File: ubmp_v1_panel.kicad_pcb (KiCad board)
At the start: 2 copper layers, 131 x 113.5 mm, 312 parts, among them J1 Conn_02x05_Counter_Clockwise, J2 USB_A, U1 NUF8401MNT4G, U2 MIC5245-3.3, U3 STM32F103CBUx, U4 NUF2042XV6T1G, Y1 PRQC8.00CR1010V00L

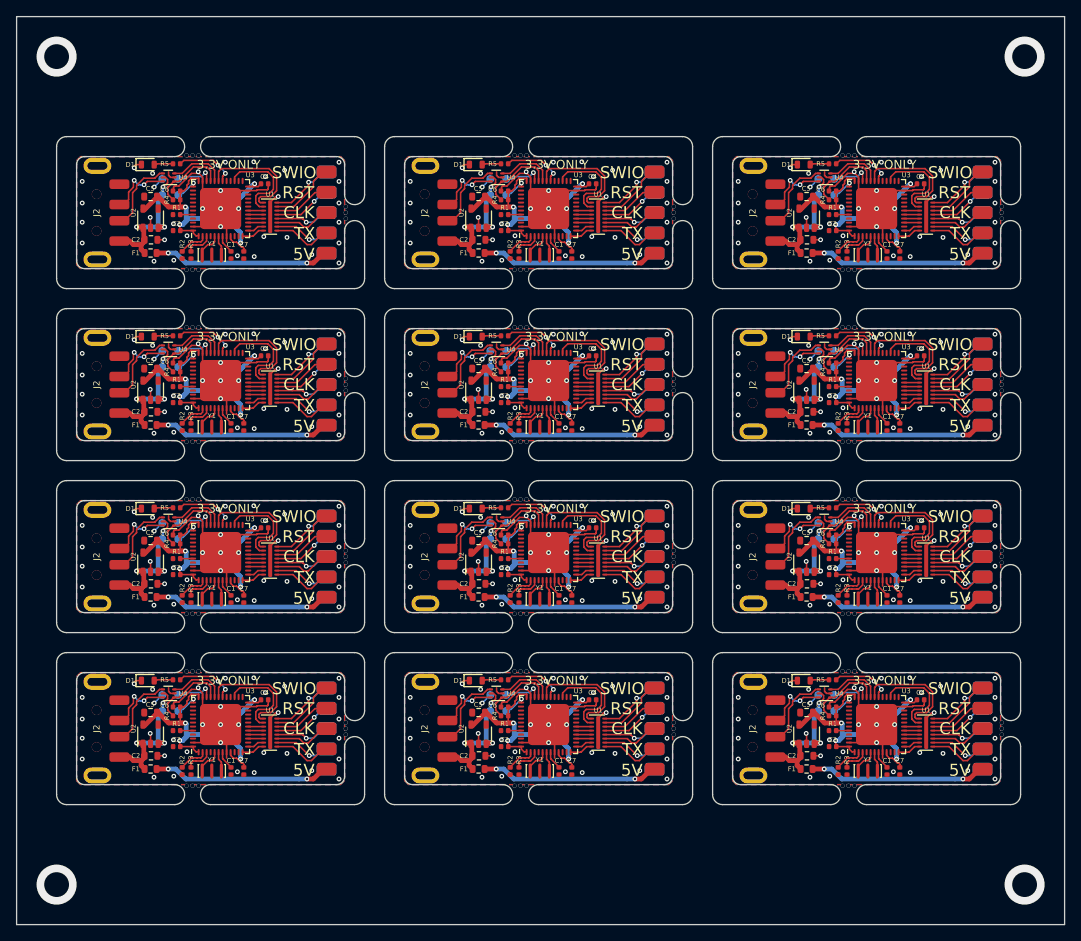
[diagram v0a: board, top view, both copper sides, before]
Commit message: Updated USBPCB version and panel
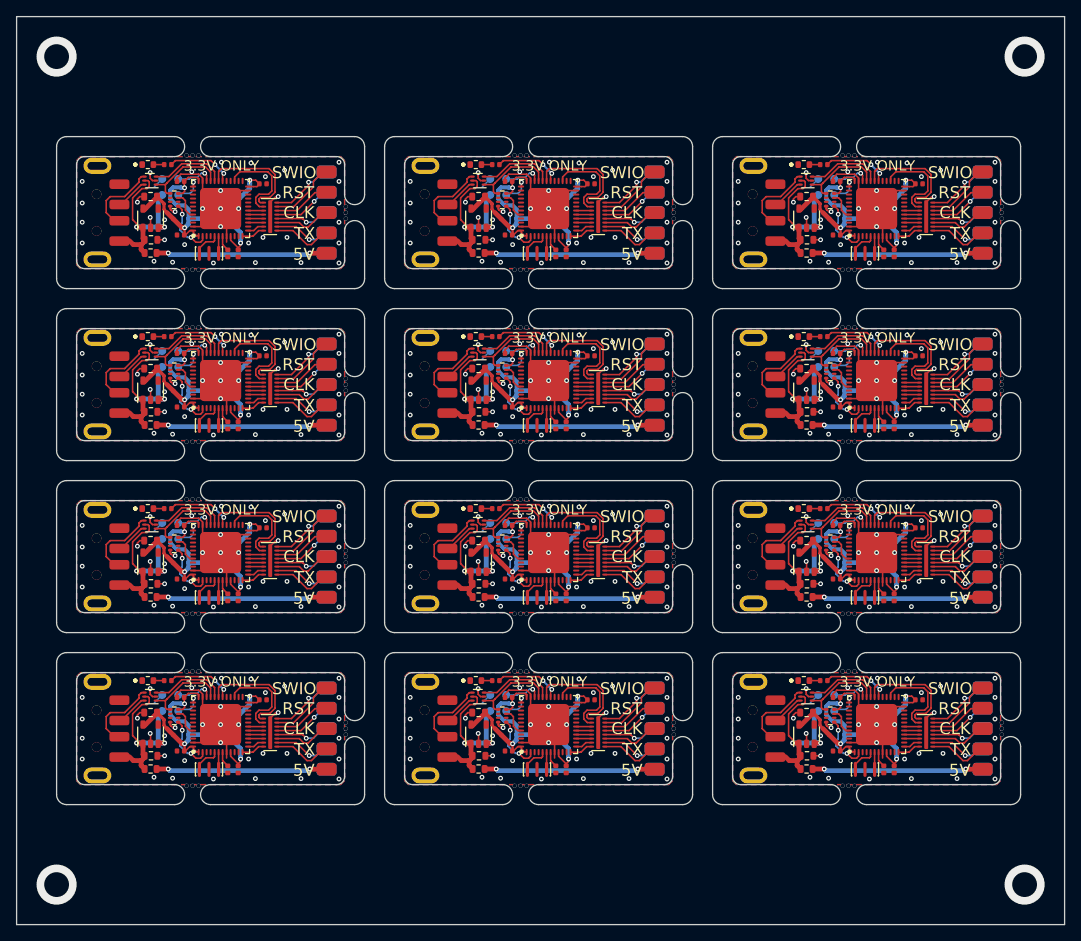
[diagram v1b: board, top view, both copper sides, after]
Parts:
- removed the C1 at (177.8, 64.3)
- removed the C1 at (177.8, 128.8)
- removed the C1 at (136.8, 128.8)
- removed the C1 at (95.8, 128.8)
- removed the C1 at (136.8, 64.3)
- removed the C1 at (95.8, 64.3)
- removed the C1 at (177.8, 85.8)
- removed the C1 at (136.8, 85.8)
- removed the C1 at (95.8, 85.8)
- removed the C1 at (177.8, 107.3)
- removed the C1 at (136.8, 107.3)
- removed the C1 at (95.8, 107.3)
- removed the C3 at (171.0, 61.2)
- removed the C3 at (171.0, 125.8)
- removed the C3 at (130.0, 125.8)
- removed the C3 at (89.0, 125.8)
- removed the C3 at (130.0, 61.2)
- removed the C3 at (89.0, 61.2)
- removed the C3 at (171.0, 82.8)
- removed the C3 at (130.0, 82.8)
- removed the C3 at (89.0, 82.8)
- removed the C3 at (171.0, 104.2)
- removed the C3 at (130.0, 104.2)
- removed the C3 at (89.0, 104.2)
- removed the C4 at (141.0, 55.4)
- removed the C4 at (182.0, 119.9)
- removed the C4 at (141.0, 119.9)
- removed the C4 at (100.0, 119.9)
- removed the C4 at (182.0, 55.4)
- removed the C4 at (100.0, 55.4)
- removed the C4 at (141.0, 76.9)
- removed the C4 at (182.0, 76.9)
- removed the C4 at (100.0, 76.9)
- removed the C4 at (141.0, 98.4)
- removed the C4 at (182.0, 98.4)
- removed the C4 at (100.0, 98.4)
- removed the C6 at (130.0, 56.3)
- removed the C6 at (171.0, 120.8)
- removed the C6 at (130.0, 120.8)
- removed the C6 at (89.0, 120.8)
- removed the C6 at (171.0, 56.3)
- removed the C6 at (89.0, 56.3)
- removed the C6 at (130.0, 77.8)
- removed the C6 at (171.0, 77.8)
- removed the C6 at (89.0, 77.8)
- removed the C6 at (130.0, 99.3)
- removed the C6 at (171.0, 99.3)
- removed the C6 at (89.0, 99.3)
- removed the C7 at (179.4, 64.3)
- removed the C7 at (179.4, 128.8)
- removed the C7 at (138.4, 128.8)
- removed the C7 at (97.4, 128.8)
- removed the C7 at (138.4, 64.3)
- removed the C7 at (97.4, 64.3)
- removed the C7 at (179.4, 85.8)
- removed the C7 at (138.4, 85.8)
- removed the C7 at (97.4, 85.8)
- removed the C7 at (179.4, 107.3)
- removed the C7 at (138.4, 107.3)
- removed the C7 at (97.4, 107.3)
- removed the D1 at (167.4, 53.0)
- removed the D1 at (167.4, 117.5)
- removed the D1 at (126.4, 117.5)
- removed the D1 at (85.4, 117.5)
- removed the D1 at (126.4, 53.0)
- removed the D1 at (85.4, 53.0)
- removed the D1 at (167.4, 74.5)
- removed the D1 at (126.4, 74.5)
- removed the D1 at (85.4, 74.5)
- removed the D1 at (167.4, 96.0)
- removed the D1 at (126.4, 96.0)
- removed the D1 at (85.4, 96.0)
- removed the R1 at (130.0, 59.2)
- removed the R1 at (171.0, 123.8)
- removed the R1 at (130.0, 123.8)
- removed the R1 at (89.0, 123.8)
- removed the R1 at (171.0, 59.2)
- removed the R1 at (89.0, 59.2)
- removed the R1 at (130.0, 80.8)
- removed the R1 at (171.0, 80.8)
- removed the R1 at (89.0, 80.8)
- removed the R1 at (130.0, 102.2)
- removed the R1 at (171.0, 102.2)
- removed the R1 at (89.0, 102.2)
- removed R2 (x12), R3 (x12), R4 (x12): 1.5k, passive:R_0402_1005Metric_Rounded
- removed R5 (x12): 470, passive:R_0402_1005Metric_Rounded
- removed the REF** at (137.5, 56.0)
- removed the REF** at (178.5, 120.5)
- removed the REF** at (137.5, 120.5)
- removed the REF** at (96.5, 120.5)
- removed the REF** at (178.5, 56.0)
- removed the REF** at (96.5, 56.0)
- removed the REF** at (137.5, 77.5)
- removed the REF** at (178.5, 77.5)
- removed the REF** at (96.5, 77.5)
- removed the REF** at (137.5, 99.0)
- removed the REF** at (178.5, 99.0)
- removed the REF** at (96.5, 99.0)
- removed the U4 at (129.0, 54.6)
- removed the U4 at (170.0, 119.1)
- removed the U4 at (129.0, 119.1)
- removed the U4 at (88.0, 119.1)
- removed the U4 at (170.0, 54.6)
- removed the U4 at (88.0, 54.6)
- removed the U4 at (129.0, 76.1)
- removed the U4 at (170.0, 76.1)
- removed the U4 at (88.0, 76.1)
- removed the U4 at (129.0, 97.6)
- removed the U4 at (170.0, 97.6)
- removed the U4 at (88.0, 97.6)
- removed the Y1 at (175.4, 64.3)
- removed the Y1 at (175.4, 128.8)
- removed the Y1 at (134.4, 128.8)
- removed the Y1 at (93.4, 128.8)
- removed the Y1 at (134.4, 64.3)
- removed the Y1 at (93.4, 64.3)
- removed the Y1 at (175.4, 85.8)
- removed the Y1 at (134.4, 85.8)
- removed the Y1 at (93.4, 85.8)
- removed the Y1 at (175.4, 107.3)
- removed the Y1 at (134.4, 107.3)
- removed the Y1 at (93.4, 107.3)
- added C1: 100n, passive:C_0402_1005Metric_Rounded, F.Cu at (95.4, 64.1)
- added C1: 100n, passive:C_0402_1005Metric_Rounded, F.Cu at (177.4, 128.6)
- added C1: 100n, passive:C_0402_1005Metric_Rounded, F.Cu at (136.4, 128.6)
- added C1: 100n, passive:C_0402_1005Metric_Rounded, F.Cu at (95.4, 128.6)
- added C1: 100n, passive:C_0402_1005Metric_Rounded, F.Cu at (136.4, 64.1)
- added C1: 100n, passive:C_0402_1005Metric_Rounded, F.Cu at (177.4, 64.1)
- added C1: 100n, passive:C_0402_1005Metric_Rounded, F.Cu at (95.4, 85.6)
- added C1: 100n, passive:C_0402_1005Metric_Rounded, F.Cu at (136.4, 85.6)
- added C1: 100n, passive:C_0402_1005Metric_Rounded, F.Cu at (177.4, 85.6)
- added C1: 100n, passive:C_0402_1005Metric_Rounded, F.Cu at (95.4, 107.1)
- added C1: 100n, passive:C_0402_1005Metric_Rounded, F.Cu at (136.4, 107.1)
- added C1: 100n, passive:C_0402_1005Metric_Rounded, F.Cu at (177.4, 107.1)
- added C3: 100n, passive:C_0402_1005Metric_Rounded, F.Cu at (130.5, 61.8)
- added C3: 100n, passive:C_0402_1005Metric_Rounded, F.Cu at (171.5, 126.3)
- added C3: 100n, passive:C_0402_1005Metric_Rounded, F.Cu at (130.5, 126.3)
- added C3: 100n, passive:C_0402_1005Metric_Rounded, F.Cu at (89.5, 126.3)
- added C3: 100n, passive:C_0402_1005Metric_Rounded, F.Cu at (89.5, 61.8)
- added C3: 100n, passive:C_0402_1005Metric_Rounded, F.Cu at (171.5, 61.8)
- added C3: 100n, passive:C_0402_1005Metric_Rounded, F.Cu at (130.5, 83.3)
- added C3: 100n, passive:C_0402_1005Metric_Rounded, F.Cu at (89.5, 83.3)
- added C3: 100n, passive:C_0402_1005Metric_Rounded, F.Cu at (171.5, 83.3)
- added C3: 100n, passive:C_0402_1005Metric_Rounded, F.Cu at (130.5, 104.8)
- added C3: 100n, passive:C_0402_1005Metric_Rounded, F.Cu at (89.5, 104.8)
- added C3: 100n, passive:C_0402_1005Metric_Rounded, F.Cu at (171.5, 104.8)
- added C4: 100n, passive:C_0402_1005Metric_Rounded, F.Cu at (140.8, 55.4)
- added C4: 100n, passive:C_0402_1005Metric_Rounded, F.Cu at (181.8, 119.9)
- added C4: 100n, passive:C_0402_1005Metric_Rounded, F.Cu at (140.8, 119.9)
- added C4: 100n, passive:C_0402_1005Metric_Rounded, F.Cu at (99.8, 119.9)
- added C4: 100n, passive:C_0402_1005Metric_Rounded, F.Cu at (99.8, 55.4)
- added C4: 100n, passive:C_0402_1005Metric_Rounded, F.Cu at (181.8, 55.4)
- added C4: 100n, passive:C_0402_1005Metric_Rounded, F.Cu at (140.8, 76.9)
- added C4: 100n, passive:C_0402_1005Metric_Rounded, F.Cu at (99.8, 76.9)
- added C4: 100n, passive:C_0402_1005Metric_Rounded, F.Cu at (181.8, 76.9)
- added C4: 100n, passive:C_0402_1005Metric_Rounded, F.Cu at (140.8, 98.4)
- added C4: 100n, passive:C_0402_1005Metric_Rounded, F.Cu at (99.8, 98.4)
- added C4: 100n, passive:C_0402_1005Metric_Rounded, F.Cu at (181.8, 98.4)
- added C6: 100n, passive:C_0402_1005Metric_Rounded, F.Cu at (89.5, 55.1)
- added C6: 100n, passive:C_0402_1005Metric_Rounded, F.Cu at (171.5, 119.6)
- added C6: 100n, passive:C_0402_1005Metric_Rounded, F.Cu at (130.5, 119.6)
- added C6: 100n, passive:C_0402_1005Metric_Rounded, F.Cu at (89.5, 119.6)
- added C6: 100n, passive:C_0402_1005Metric_Rounded, F.Cu at (171.5, 55.1)
- added C6: 100n, passive:C_0402_1005Metric_Rounded, F.Cu at (130.5, 55.1)
- added C6: 100n, passive:C_0402_1005Metric_Rounded, F.Cu at (89.5, 76.6)
- added C6: 100n, passive:C_0402_1005Metric_Rounded, F.Cu at (171.5, 76.6)
- added C6: 100n, passive:C_0402_1005Metric_Rounded, F.Cu at (130.5, 76.6)
- added C6: 100n, passive:C_0402_1005Metric_Rounded, F.Cu at (89.5, 98.1)
- added C6: 100n, passive:C_0402_1005Metric_Rounded, F.Cu at (171.5, 98.1)
- added C6: 100n, passive:C_0402_1005Metric_Rounded, F.Cu at (130.5, 98.1)
- added C7: 100n, passive:C_0402_1005Metric_Rounded, F.Cu at (96.7, 64.1)
- added C7: 100n, passive:C_0402_1005Metric_Rounded, F.Cu at (178.7, 128.6)
- added C7: 100n, passive:C_0402_1005Metric_Rounded, F.Cu at (137.7, 128.6)
- added C7: 100n, passive:C_0402_1005Metric_Rounded, F.Cu at (96.7, 128.6)
- added C7: 100n, passive:C_0402_1005Metric_Rounded, F.Cu at (178.7, 64.1)
- added C7: 100n, passive:C_0402_1005Metric_Rounded, F.Cu at (137.7, 64.1)
- added C7: 100n, passive:C_0402_1005Metric_Rounded, F.Cu at (96.7, 85.6)
- added C7: 100n, passive:C_0402_1005Metric_Rounded, F.Cu at (178.7, 85.6)
- added C7: 100n, passive:C_0402_1005Metric_Rounded, F.Cu at (137.7, 85.6)
- added C7: 100n, passive:C_0402_1005Metric_Rounded, F.Cu at (96.7, 107.1)
- added C7: 100n, passive:C_0402_1005Metric_Rounded, F.Cu at (178.7, 107.1)
- added C7: 100n, passive:C_0402_1005Metric_Rounded, F.Cu at (137.7, 107.1)
- added D1: GREEN, leds:LEDC1608X60, F.Cu at (85.4, 53.0)
- added D1: GREEN, leds:LEDC1608X60, F.Cu at (167.4, 117.5)
- added D1: GREEN, leds:LEDC1608X60, F.Cu at (126.4, 117.5)
- added D1: GREEN, leds:LEDC1608X60, F.Cu at (85.4, 117.5)
- added D1: GREEN, leds:LEDC1608X60, F.Cu at (167.4, 53.0)
- added D1: GREEN, leds:LEDC1608X60, F.Cu at (126.4, 53.0)
- added D1: GREEN, leds:LEDC1608X60, F.Cu at (85.4, 74.5)
- added D1: GREEN, leds:LEDC1608X60, F.Cu at (167.4, 74.5)
- added D1: GREEN, leds:LEDC1608X60, F.Cu at (126.4, 74.5)
- added D1: GREEN, leds:LEDC1608X60, F.Cu at (85.4, 96.0)
- added D1: GREEN, leds:LEDC1608X60, F.Cu at (167.4, 96.0)
- added D1: GREEN, leds:LEDC1608X60, F.Cu at (126.4, 96.0)
- added R1: 470, passive:R_0402_1005Metric_Rounded, F.Cu at (87.9, 53.0)
- added R1: 470, passive:R_0402_1005Metric_Rounded, F.Cu at (169.9, 117.5)
- added R1: 470, passive:R_0402_1005Metric_Rounded, F.Cu at (128.9, 117.5)
- added R1: 470, passive:R_0402_1005Metric_Rounded, F.Cu at (87.9, 117.5)
- added R1: 470, passive:R_0402_1005Metric_Rounded, F.Cu at (169.9, 53.0)
- added R1: 470, passive:R_0402_1005Metric_Rounded, F.Cu at (128.9, 53.0)
- added R1: 470, passive:R_0402_1005Metric_Rounded, F.Cu at (87.9, 74.5)
- added R1: 470, passive:R_0402_1005Metric_Rounded, F.Cu at (169.9, 74.5)
- added R1: 470, passive:R_0402_1005Metric_Rounded, F.Cu at (128.9, 74.5)
- added R1: 470, passive:R_0402_1005Metric_Rounded, F.Cu at (87.9, 96.0)
- added R1: 470, passive:R_0402_1005Metric_Rounded, F.Cu at (169.9, 96.0)
- added R1: 470, passive:R_0402_1005Metric_Rounded, F.Cu at (128.9, 96.0)
- added REF**: OSHW-Symbol_6.7x6mm_SilkScreen, Symbol:OSHW-Symbol_6.7x6mm_SilkScreen, B.Cu at (97.6, 55.7)
- added REF**: OSHW-Symbol_6.7x6mm_SilkScreen, Symbol:OSHW-Symbol_6.7x6mm_SilkScreen, B.Cu at (179.6, 120.2)
- added REF**: OSHW-Symbol_6.7x6mm_SilkScreen, Symbol:OSHW-Symbol_6.7x6mm_SilkScreen, B.Cu at (138.6, 120.2)
- added REF**: OSHW-Symbol_6.7x6mm_SilkScreen, Symbol:OSHW-Symbol_6.7x6mm_SilkScreen, B.Cu at (97.6, 120.2)
- added REF**: OSHW-Symbol_6.7x6mm_SilkScreen, Symbol:OSHW-Symbol_6.7x6mm_SilkScreen, B.Cu at (138.6, 55.7)
- added REF**: OSHW-Symbol_6.7x6mm_SilkScreen, Symbol:OSHW-Symbol_6.7x6mm_SilkScreen, B.Cu at (179.6, 55.7)
- added REF**: OSHW-Symbol_6.7x6mm_SilkScreen, Symbol:OSHW-Symbol_6.7x6mm_SilkScreen, B.Cu at (97.6, 77.2)
- added REF**: OSHW-Symbol_6.7x6mm_SilkScreen, Symbol:OSHW-Symbol_6.7x6mm_SilkScreen, B.Cu at (138.6, 77.2)
- added REF**: OSHW-Symbol_6.7x6mm_SilkScreen, Symbol:OSHW-Symbol_6.7x6mm_SilkScreen, B.Cu at (179.6, 77.2)
- added REF**: OSHW-Symbol_6.7x6mm_SilkScreen, Symbol:OSHW-Symbol_6.7x6mm_SilkScreen, B.Cu at (97.6, 98.7)
- added REF**: OSHW-Symbol_6.7x6mm_SilkScreen, Symbol:OSHW-Symbol_6.7x6mm_SilkScreen, B.Cu at (138.6, 98.7)
- added REF**: OSHW-Symbol_6.7x6mm_SilkScreen, Symbol:OSHW-Symbol_6.7x6mm_SilkScreen, B.Cu at (179.6, 98.7)
- added RN1: 1.5k, passive:R_Array_Convex_4x0402, F.Cu at (129.7, 57.4)
- added RN1: 1.5k, passive:R_Array_Convex_4x0402, F.Cu at (170.7, 121.9)
- added RN1: 1.5k, passive:R_Array_Convex_4x0402, F.Cu at (129.7, 121.9)
- added RN1: 1.5k, passive:R_Array_Convex_4x0402, F.Cu at (88.7, 121.9)
- added RN1: 1.5k, passive:R_Array_Convex_4x0402, F.Cu at (88.7, 57.4)
- added RN1: 1.5k, passive:R_Array_Convex_4x0402, F.Cu at (170.7, 57.4)
- added RN1: 1.5k, passive:R_Array_Convex_4x0402, F.Cu at (129.7, 78.9)
- added RN1: 1.5k, passive:R_Array_Convex_4x0402, F.Cu at (88.7, 78.9)
- added RN1: 1.5k, passive:R_Array_Convex_4x0402, F.Cu at (170.7, 78.9)
- added RN1: 1.5k, passive:R_Array_Convex_4x0402, F.Cu at (129.7, 100.4)
- added RN1: 1.5k, passive:R_Array_Convex_4x0402, F.Cu at (88.7, 100.4)
- added RN1: 1.5k, passive:R_Array_Convex_4x0402, F.Cu at (170.7, 100.4)
- added U4: NUF2042XV6T1G, dfn:DFN-6-1EP_1.2x1.6mm_P0.5mm, F.Cu at (126.7, 55.0)
- added U4: NUF2042XV6T1G, dfn:DFN-6-1EP_1.2x1.6mm_P0.5mm, F.Cu at (167.7, 119.5)
- added U4: NUF2042XV6T1G, dfn:DFN-6-1EP_1.2x1.6mm_P0.5mm, F.Cu at (126.7, 119.5)
- added U4: NUF2042XV6T1G, dfn:DFN-6-1EP_1.2x1.6mm_P0.5mm, F.Cu at (85.7, 119.5)
- added U4: NUF2042XV6T1G, dfn:DFN-6-1EP_1.2x1.6mm_P0.5mm, F.Cu at (85.7, 55.0)
- added U4: NUF2042XV6T1G, dfn:DFN-6-1EP_1.2x1.6mm_P0.5mm, F.Cu at (167.7, 55.0)
- added U4: NUF2042XV6T1G, dfn:DFN-6-1EP_1.2x1.6mm_P0.5mm, F.Cu at (126.7, 76.5)
- added U4: NUF2042XV6T1G, dfn:DFN-6-1EP_1.2x1.6mm_P0.5mm, F.Cu at (85.7, 76.5)
- added U4: NUF2042XV6T1G, dfn:DFN-6-1EP_1.2x1.6mm_P0.5mm, F.Cu at (167.7, 76.5)
- added U4: NUF2042XV6T1G, dfn:DFN-6-1EP_1.2x1.6mm_P0.5mm, F.Cu at (126.7, 98.0)
- added U4: NUF2042XV6T1G, dfn:DFN-6-1EP_1.2x1.6mm_P0.5mm, F.Cu at (85.7, 98.0)
- added U4: NUF2042XV6T1G, dfn:DFN-6-1EP_1.2x1.6mm_P0.5mm, F.Cu at (167.7, 98.0)
- added Y1: PRQC8.00CR1010V00L, crystals:Resonator_3pin_3.2x1.3mm, F.Cu at (134.1, 64.1)
- added Y1: PRQC8.00CR1010V00L, crystals:Resonator_3pin_3.2x1.3mm, F.Cu at (175.1, 128.6)
- added Y1: PRQC8.00CR1010V00L, crystals:Resonator_3pin_3.2x1.3mm, F.Cu at (134.1, 128.6)
- added Y1: PRQC8.00CR1010V00L, crystals:Resonator_3pin_3.2x1.3mm, F.Cu at (93.0, 128.6)
- added Y1: PRQC8.00CR1010V00L, crystals:Resonator_3pin_3.2x1.3mm, F.Cu at (93.0, 64.1)
- added Y1: PRQC8.00CR1010V00L, crystals:Resonator_3pin_3.2x1.3mm, F.Cu at (175.1, 64.1)
- added Y1: PRQC8.00CR1010V00L, crystals:Resonator_3pin_3.2x1.3mm, F.Cu at (134.1, 85.6)
- added Y1: PRQC8.00CR1010V00L, crystals:Resonator_3pin_3.2x1.3mm, F.Cu at (93.0, 85.6)
- added Y1: PRQC8.00CR1010V00L, crystals:Resonator_3pin_3.2x1.3mm, F.Cu at (175.1, 85.6)
- added Y1: PRQC8.00CR1010V00L, crystals:Resonator_3pin_3.2x1.3mm, F.Cu at (134.1, 107.1)
- added Y1: PRQC8.00CR1010V00L, crystals:Resonator_3pin_3.2x1.3mm, F.Cu at (93.0, 107.1)
- added Y1: PRQC8.00CR1010V00L, crystals:Resonator_3pin_3.2x1.3mm, F.Cu at (175.1, 107.1)
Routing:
- net (no net): track 3416.0 -> 3511.9 mm

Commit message: Updated panel for hand assembly
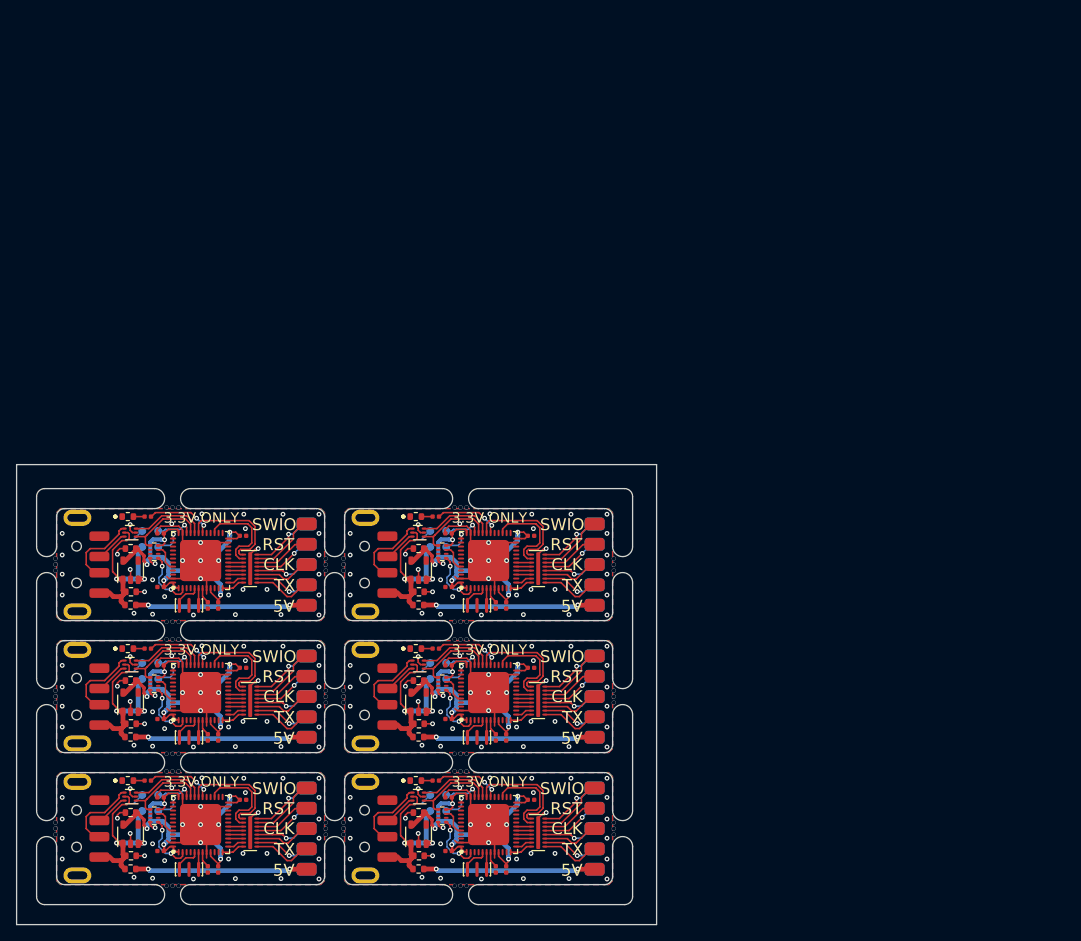
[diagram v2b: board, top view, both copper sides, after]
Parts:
- removed the C1 at (95.4, 64.1)
- removed the C1 at (177.4, 128.6)
- removed the C1 at (136.4, 128.6)
- removed the C1 at (95.4, 128.6)
- removed the C1 at (136.4, 64.1)
- removed the C1 at (177.4, 64.1)
- removed the C1 at (95.4, 85.6)
- removed the C1 at (136.4, 85.6)
- removed the C1 at (177.4, 85.6)
- removed the C1 at (95.4, 107.1)
- removed the C1 at (136.4, 107.1)
- removed the C1 at (177.4, 107.1)
- removed the C2 at (126.8, 62.4)
- removed the C2 at (167.8, 126.9)
- removed the C2 at (126.8, 126.9)
- removed the C2 at (85.8, 126.9)
- removed the C2 at (167.8, 62.4)
- removed the C2 at (85.8, 62.4)
- removed the C2 at (126.8, 83.9)
- removed the C2 at (167.8, 83.9)
- removed the C2 at (85.8, 83.9)
- removed the C2 at (126.8, 105.4)
- removed the C2 at (167.8, 105.4)
- removed the C2 at (85.8, 105.4)
- removed the C3 at (130.5, 61.8)
- removed the C3 at (171.5, 126.3)
- removed the C3 at (130.5, 126.3)
- removed the C3 at (89.5, 126.3)
- removed the C3 at (89.5, 61.8)
- removed the C3 at (171.5, 61.8)
- removed the C3 at (130.5, 83.3)
- removed the C3 at (89.5, 83.3)
- removed the C3 at (171.5, 83.3)
- removed the C3 at (130.5, 104.8)
- removed the C3 at (89.5, 104.8)
- removed the C3 at (171.5, 104.8)
- removed the C4 at (140.8, 55.4)
- removed the C4 at (181.8, 119.9)
- removed the C4 at (140.8, 119.9)
- removed the C4 at (99.8, 119.9)
- removed the C4 at (99.8, 55.4)
- removed the C4 at (181.8, 55.4)
- removed the C4 at (140.8, 76.9)
- removed the C4 at (99.8, 76.9)
- removed the C4 at (181.8, 76.9)
- removed the C4 at (140.8, 98.4)
- removed the C4 at (99.8, 98.4)
- removed the C4 at (181.8, 98.4)
- removed the C5 at (126.8, 57.0)
- removed the C5 at (167.8, 121.5)
- removed the C5 at (126.8, 121.5)
- removed the C5 at (85.8, 121.5)
- removed the C5 at (85.8, 57.0)
- removed the C5 at (167.8, 57.0)
- removed the C5 at (126.8, 78.5)
- removed the C5 at (85.8, 78.5)
- removed the C5 at (167.8, 78.5)
- removed the C5 at (126.8, 100.0)
- removed the C5 at (85.8, 100.0)
- removed the C5 at (167.8, 100.0)
- removed the C6 at (89.5, 55.1)
- removed the C6 at (171.5, 119.6)
- removed the C6 at (130.5, 119.6)
- removed the C6 at (89.5, 119.6)
- removed the C6 at (171.5, 55.1)
- removed the C6 at (130.5, 55.1)
- removed the C6 at (89.5, 76.6)
- removed the C6 at (171.5, 76.6)
- removed the C6 at (130.5, 76.6)
- removed the C6 at (89.5, 98.1)
- removed the C6 at (171.5, 98.1)
- removed the C6 at (130.5, 98.1)
- removed the C7 at (96.7, 64.1)
- removed the C7 at (178.7, 128.6)
- removed the C7 at (137.7, 128.6)
- removed the C7 at (96.7, 128.6)
- removed the C7 at (178.7, 64.1)
- removed the C7 at (137.7, 64.1)
- removed the C7 at (96.7, 85.6)
- removed the C7 at (178.7, 85.6)
- removed the C7 at (137.7, 85.6)
- removed the C7 at (96.7, 107.1)
- removed the C7 at (178.7, 107.1)
- removed the C7 at (137.7, 107.1)
- removed the D1 at (85.4, 53.0)
- removed the D1 at (167.4, 117.5)
- removed the D1 at (126.4, 117.5)
- removed the D1 at (85.4, 117.5)
- removed the D1 at (167.4, 53.0)
- removed the D1 at (126.4, 53.0)
- removed the D1 at (85.4, 74.5)
- removed the D1 at (167.4, 74.5)
- removed the D1 at (126.4, 74.5)
- removed the D1 at (85.4, 96.0)
- removed the D1 at (167.4, 96.0)
- removed the D1 at (126.4, 96.0)
- removed the F1 at (167.8, 64.0)
- removed the F1 at (167.8, 128.6)
- removed the F1 at (126.8, 128.6)
- removed the F1 at (85.8, 128.6)
- removed the F1 at (85.8, 64.0)
- removed the F1 at (126.8, 64.0)
- removed the F1 at (167.8, 85.5)
- removed the F1 at (85.8, 85.5)
- removed the F1 at (126.8, 85.5)
- removed the F1 at (167.8, 107.0)
- removed the F1 at (85.8, 107.0)
- removed the F1 at (126.8, 107.0)
- removed the J1 at (148.8, 59.0)
- removed the J1 at (189.8, 123.5)
- removed the J1 at (148.8, 123.5)
- removed the J1 at (107.8, 123.5)
- removed the J1 at (107.8, 59.0)
- removed the J1 at (189.8, 59.0)
- removed the J1 at (148.8, 80.5)
- removed the J1 at (107.8, 80.5)
- removed the J1 at (189.8, 80.5)
- removed the J1 at (148.8, 102.0)
- removed the J1 at (107.8, 102.0)
- removed the J1 at (189.8, 102.0)
- removed the J2 at (81.1, 59.0)
- removed the J2 at (163.1, 123.5)
- removed the J2 at (122.1, 123.5)
- removed the J2 at (81.1, 123.5)
- removed the J2 at (163.1, 59.0)
- removed the J2 at (122.1, 59.0)
- removed the J2 at (81.1, 80.5)
- removed the J2 at (163.1, 80.5)
- removed the J2 at (122.1, 80.5)
- removed the J2 at (81.1, 102.0)
- removed the J2 at (163.1, 102.0)
- removed the J2 at (122.1, 102.0)
- removed the R1 at (87.9, 53.0)
- removed the R1 at (169.9, 117.5)
- removed the R1 at (128.9, 117.5)
- removed the R1 at (87.9, 117.5)
- removed the R1 at (169.9, 53.0)
- removed the R1 at (128.9, 53.0)
- removed the R1 at (87.9, 74.5)
- removed the R1 at (169.9, 74.5)
- removed the R1 at (128.9, 74.5)
- removed the R1 at (87.9, 96.0)
- removed the R1 at (169.9, 96.0)
- removed the R1 at (128.9, 96.0)
- removed the REF** at (97.6, 55.7)
- removed the REF** at (179.6, 120.2)
- removed the REF** at (138.6, 120.2)
- removed the REF** at (97.6, 120.2)
- removed the REF** at (138.6, 55.7)
- removed the REF** at (179.6, 55.7)
- removed the REF** at (97.6, 77.2)
- removed the REF** at (138.6, 77.2)
- removed the REF** at (179.6, 77.2)
- removed the REF** at (97.6, 98.7)
- removed the REF** at (138.6, 98.7)
- removed the REF** at (179.6, 98.7)
- removed the RN1 at (129.7, 57.4)
- removed the RN1 at (170.7, 121.9)
- removed the RN1 at (129.7, 121.9)
- removed the RN1 at (88.7, 121.9)
- removed the RN1 at (88.7, 57.4)
- removed the RN1 at (170.7, 57.4)
- removed the RN1 at (129.7, 78.9)
- removed the RN1 at (88.7, 78.9)
- removed the RN1 at (170.7, 78.9)
- removed the RN1 at (129.7, 100.4)
- removed the RN1 at (88.7, 100.4)
- removed the RN1 at (170.7, 100.4)
- removed the TP1 at (130.2, 54.8)
- removed the TP1 at (171.2, 119.3)
- removed the TP1 at (130.2, 119.3)
- removed the TP1 at (89.2, 119.3)
- removed the TP1 at (89.2, 54.8)
- removed the TP1 at (171.2, 54.8)
- removed the TP1 at (130.2, 76.3)
- removed the TP1 at (89.2, 76.3)
- removed the TP1 at (171.2, 76.3)
- removed the TP1 at (130.2, 97.8)
- removed the TP1 at (89.2, 97.8)
- removed the TP1 at (171.2, 97.8)
- removed the TP2 at (130.2, 56.8)
- removed the TP2 at (171.2, 121.3)
- removed the TP2 at (130.2, 121.3)
- removed the TP2 at (89.2, 121.3)
- removed the TP2 at (89.2, 56.8)
- removed the TP2 at (171.2, 56.8)
- removed the TP2 at (130.2, 78.3)
- removed the TP2 at (89.2, 78.3)
- removed the TP2 at (171.2, 78.3)
- removed the TP2 at (130.2, 99.8)
- removed the TP2 at (89.2, 99.8)
- removed the TP2 at (171.2, 99.8)
- removed the TP3 at (169.2, 54.8)
- removed the TP3 at (169.2, 119.3)
- removed the TP3 at (128.2, 119.3)
- removed the TP3 at (87.2, 119.3)
- removed the TP3 at (128.2, 54.8)
- removed the TP3 at (87.2, 54.8)
- removed the TP3 at (169.2, 76.3)
- removed the TP3 at (128.2, 76.3)
- removed the TP3 at (87.2, 76.3)
- removed the TP3 at (169.2, 97.8)
- removed the TP3 at (128.2, 97.8)
- removed the TP3 at (87.2, 97.8)
- removed the TP4 at (169.2, 56.8)
- removed the TP4 at (169.2, 121.3)
- removed the TP4 at (128.2, 121.3)
- removed the TP4 at (87.2, 121.3)
- removed the TP4 at (128.2, 56.8)
- removed the TP4 at (87.2, 56.8)
- removed the TP4 at (169.2, 78.3)
- removed the TP4 at (128.2, 78.3)
- removed the TP4 at (87.2, 78.3)
- removed the TP4 at (169.2, 99.8)
- removed the TP4 at (128.2, 99.8)
- removed the TP4 at (87.2, 99.8)
- removed the U1 at (100.7, 59.5)
- removed the U1 at (182.7, 124.0)
- removed the U1 at (141.7, 124.0)
- removed the U1 at (100.7, 124.0)
- removed the U1 at (182.7, 59.5)
- removed the U1 at (141.7, 59.5)
- removed the U1 at (100.7, 81.0)
- removed the U1 at (182.7, 81.0)
- removed the U1 at (141.7, 81.0)
- removed the U1 at (100.7, 102.5)
- removed the U1 at (182.7, 102.5)
- removed the U1 at (141.7, 102.5)
- removed the U2 at (167.8, 59.7)
- removed the U2 at (167.8, 124.2)
- removed the U2 at (126.8, 124.2)
- removed the U2 at (85.8, 124.2)
- removed the U2 at (85.8, 59.7)
- removed the U2 at (126.8, 59.7)
- removed the U2 at (167.8, 81.2)
- removed the U2 at (85.8, 81.2)
- removed the U2 at (126.8, 81.2)
- removed the U2 at (167.8, 102.7)
- removed the U2 at (85.8, 102.7)
- removed the U2 at (126.8, 102.7)
- removed the U3 at (135.5, 58.5)
- removed the U3 at (176.5, 123.0)
- removed the U3 at (135.5, 123.0)
- removed the U3 at (94.5, 123.0)
- removed the U3 at (94.5, 58.5)
- removed the U3 at (176.5, 58.5)
- removed the U3 at (135.5, 80.0)
- removed the U3 at (94.5, 80.0)
- removed the U3 at (176.5, 80.0)
- removed the U3 at (135.5, 101.5)
- removed the U3 at (94.5, 101.5)
- removed the U3 at (176.5, 101.5)
- removed the U4 at (126.7, 55.0)
- removed the U4 at (167.7, 119.5)
- removed the U4 at (126.7, 119.5)
- removed the U4 at (85.7, 119.5)
- removed the U4 at (85.7, 55.0)
- removed the U4 at (167.7, 55.0)
- removed the U4 at (126.7, 76.5)
- removed the U4 at (85.7, 76.5)
- removed the U4 at (167.7, 76.5)
- removed the U4 at (126.7, 98.0)
- removed the U4 at (85.7, 98.0)
- removed the U4 at (167.7, 98.0)
- removed the Y1 at (134.1, 64.1)
- removed the Y1 at (175.1, 128.6)
- removed the Y1 at (134.1, 128.6)
- removed the Y1 at (93.0, 128.6)
- removed the Y1 at (93.0, 64.1)
- removed the Y1 at (175.1, 64.1)
- removed the Y1 at (134.1, 85.6)
- removed the Y1 at (93.0, 85.6)
- removed the Y1 at (175.1, 85.6)
- removed the Y1 at (134.1, 107.1)
- removed the Y1 at (93.0, 107.1)
- removed the Y1 at (175.1, 107.1)
- added C1: 100n, passive:C_0402_1005Metric_Rounded, F.Cu at (128.9, 124.6)
- added C1: 100n, passive:C_0402_1005Metric_Rounded, F.Cu at (128.9, 108.1)
- added C1: 100n, passive:C_0402_1005Metric_Rounded, F.Cu at (128.9, 141.1)
- added C1: 100n, passive:C_0402_1005Metric_Rounded, F.Cu at (92.9, 108.1)
- added C1: 100n, passive:C_0402_1005Metric_Rounded, F.Cu at (92.9, 124.6)
- added C1: 100n, passive:C_0402_1005Metric_Rounded, F.Cu at (92.9, 141.1)
- added C2: 4.7u, passive:C_0603_1608Metric_Rounded, F.Cu at (119.3, 106.4)
- added C2: 4.7u, passive:C_0603_1608Metric_Rounded, F.Cu at (119.3, 122.9)
- added C2: 4.7u, passive:C_0603_1608Metric_Rounded, F.Cu at (119.3, 139.4)
- added C2: 4.7u, passive:C_0603_1608Metric_Rounded, F.Cu at (83.3, 106.4)
- added C2: 4.7u, passive:C_0603_1608Metric_Rounded, F.Cu at (83.3, 122.9)
- added C2: 4.7u, passive:C_0603_1608Metric_Rounded, F.Cu at (83.3, 139.4)
- added C3: 100n, passive:C_0402_1005Metric_Rounded, F.Cu at (123.0, 122.3)
- added C3: 100n, passive:C_0402_1005Metric_Rounded, F.Cu at (123.0, 105.8)
- added C3: 100n, passive:C_0402_1005Metric_Rounded, F.Cu at (123.0, 138.8)
- added C3: 100n, passive:C_0402_1005Metric_Rounded, F.Cu at (87.0, 105.8)
- added C3: 100n, passive:C_0402_1005Metric_Rounded, F.Cu at (87.0, 122.3)
- added C3: 100n, passive:C_0402_1005Metric_Rounded, F.Cu at (87.0, 138.8)
- added C4: 100n, passive:C_0402_1005Metric_Rounded, F.Cu at (133.3, 132.4)
- added C4: 100n, passive:C_0402_1005Metric_Rounded, F.Cu at (133.3, 115.9)
- added C4: 100n, passive:C_0402_1005Metric_Rounded, F.Cu at (133.3, 99.4)
- added C4: 100n, passive:C_0402_1005Metric_Rounded, F.Cu at (97.3, 99.4)
- added C4: 100n, passive:C_0402_1005Metric_Rounded, F.Cu at (97.3, 115.9)
- added C4: 100n, passive:C_0402_1005Metric_Rounded, F.Cu at (97.3, 132.4)
- added C5: 4.7u, passive:C_0603_1608Metric_Rounded, F.Cu at (119.2, 134.0)
- added C5: 4.7u, passive:C_0603_1608Metric_Rounded, F.Cu at (119.2, 117.5)
- added C5: 4.7u, passive:C_0603_1608Metric_Rounded, F.Cu at (119.2, 101.0)
- added C5: 4.7u, passive:C_0603_1608Metric_Rounded, F.Cu at (83.2, 101.0)
- added C5: 4.7u, passive:C_0603_1608Metric_Rounded, F.Cu at (83.2, 117.5)
- added C5: 4.7u, passive:C_0603_1608Metric_Rounded, F.Cu at (83.2, 134.0)
- added C6: 100n, passive:C_0402_1005Metric_Rounded, F.Cu at (123.0, 132.1)
- added C6: 100n, passive:C_0402_1005Metric_Rounded, F.Cu at (123.0, 99.1)
- added C6: 100n, passive:C_0402_1005Metric_Rounded, F.Cu at (123.0, 115.6)
- added C6: 100n, passive:C_0402_1005Metric_Rounded, F.Cu at (87.0, 99.1)
- added C6: 100n, passive:C_0402_1005Metric_Rounded, F.Cu at (87.0, 115.6)
- added C6: 100n, passive:C_0402_1005Metric_Rounded, F.Cu at (87.0, 132.1)
- added C7: 100n, passive:C_0402_1005Metric_Rounded, F.Cu at (130.2, 141.1)
- added C7: 100n, passive:C_0402_1005Metric_Rounded, F.Cu at (130.2, 124.6)
- added C7: 100n, passive:C_0402_1005Metric_Rounded, F.Cu at (130.2, 108.1)
- added C7: 100n, passive:C_0402_1005Metric_Rounded, F.Cu at (94.2, 108.1)
- added C7: 100n, passive:C_0402_1005Metric_Rounded, F.Cu at (94.2, 124.6)
- added C7: 100n, passive:C_0402_1005Metric_Rounded, F.Cu at (94.2, 141.1)
- added D1: LTST-C191KGKT, leds:LEDC1608X60, F.Cu at (118.9, 97.0)
- added D1: LTST-C191KGKT, leds:LEDC1608X60, F.Cu at (118.9, 130.0)
- added D1: LTST-C191KGKT, leds:LEDC1608X60, F.Cu at (118.9, 113.5)
- added D1: LTST-C191KGKT, leds:LEDC1608X60, F.Cu at (82.9, 97.0)
- added D1: LTST-C191KGKT, leds:LEDC1608X60, F.Cu at (82.9, 113.5)
- added D1: LTST-C191KGKT, leds:LEDC1608X60, F.Cu at (82.9, 130.0)
- added F1: MF-FSMF050X-2, passive:R_0603_1608Metric_Rounded, F.Cu at (119.2, 108.0)
- added F1: MF-FSMF050X-2, passive:R_0603_1608Metric_Rounded, F.Cu at (119.2, 124.5)
- added F1: MF-FSMF050X-2, passive:R_0603_1608Metric_Rounded, F.Cu at (119.2, 141.1)
- added F1: MF-FSMF050X-2, passive:R_0603_1608Metric_Rounded, F.Cu at (83.2, 108.0)
- added F1: MF-FSMF050X-2, passive:R_0603_1608Metric_Rounded, F.Cu at (83.2, 124.5)
- added F1: MF-FSMF050X-2, passive:R_0603_1608Metric_Rounded, F.Cu at (83.2, 141.1)
- added J1: M20-9760542, connectors:2x5_2.54mm_side, F.Cu at (141.2, 136.0)
- added J1: M20-9760542, connectors:2x5_2.54mm_side, F.Cu at (141.2, 119.5)
- added J1: M20-9760542, connectors:2x5_2.54mm_side, F.Cu at (141.2, 103.0)
- added J1: M20-9760542, connectors:2x5_2.54mm_side, F.Cu at (105.2, 103.0)
- added J1: M20-9760542, connectors:2x5_2.54mm_side, F.Cu at (105.2, 119.5)
- added J1: M20-9760542, connectors:2x5_2.54mm_side, F.Cu at (105.2, 136.0)
- added J2: 1001-011-01101, usb:USB_A_1001-011-01101, F.Cu at (114.6, 103.0)
- added J2: 1001-011-01101, usb:USB_A_1001-011-01101, F.Cu at (114.6, 136.0)
- added J2: 1001-011-01101, usb:USB_A_1001-011-01101, F.Cu at (114.6, 119.5)
- added J2: 1001-011-01101, usb:USB_A_1001-011-01101, F.Cu at (78.6, 103.0)
- added J2: 1001-011-01101, usb:USB_A_1001-011-01101, F.Cu at (78.6, 119.5)
- added J2: 1001-011-01101, usb:USB_A_1001-011-01101, F.Cu at (78.6, 136.0)
- added R1: 470, passive:R_0402_1005Metric_Rounded, F.Cu at (121.4, 113.5)
- added R1: 470, passive:R_0402_1005Metric_Rounded, F.Cu at (121.4, 97.0)
- added R1: 470, passive:R_0402_1005Metric_Rounded, F.Cu at (121.4, 130.0)
- added R1: 470, passive:R_0402_1005Metric_Rounded, F.Cu at (85.4, 97.0)
- added R1: 470, passive:R_0402_1005Metric_Rounded, F.Cu at (85.4, 113.5)
- added R1: 470, passive:R_0402_1005Metric_Rounded, F.Cu at (85.4, 130.0)
- added REF**: OSHW-Symbol_6.7x6mm_SilkScreen, Symbol:OSHW-Symbol_6.7x6mm_SilkScreen, B.Cu at (130.0, 99.5)
- added REF**: OSHW-Symbol_6.7x6mm_SilkScreen, Symbol:OSHW-Symbol_6.7x6mm_SilkScreen, B.Cu at (94.0, 99.5)
- added REF**: OSHW-Symbol_6.7x6mm_SilkScreen, Symbol:OSHW-Symbol_6.7x6mm_SilkScreen, B.Cu at (130.0, 116.0)
- added REF**: OSHW-Symbol_6.7x6mm_SilkScreen, Symbol:OSHW-Symbol_6.7x6mm_SilkScreen, B.Cu at (94.0, 116.0)
- added REF**: OSHW-Symbol_6.7x6mm_SilkScreen, Symbol:OSHW-Symbol_6.7x6mm_SilkScreen, B.Cu at (130.0, 132.5)
- added REF**: OSHW-Symbol_6.7x6mm_SilkScreen, Symbol:OSHW-Symbol_6.7x6mm_SilkScreen, B.Cu at (94.0, 132.5)
- added RN1: EXB-28V152JX, passive:R_Array_Convex_4x0402, F.Cu at (122.2, 134.4)
- added RN1: EXB-28V152JX, passive:R_Array_Convex_4x0402, F.Cu at (122.2, 101.4)
- added RN1: EXB-28V152JX, passive:R_Array_Convex_4x0402, F.Cu at (122.2, 117.9)
- added RN1: EXB-28V152JX, passive:R_Array_Convex_4x0402, F.Cu at (86.2, 101.4)
- added RN1: EXB-28V152JX, passive:R_Array_Convex_4x0402, F.Cu at (86.2, 117.9)
- added RN1: EXB-28V152JX, passive:R_Array_Convex_4x0402, F.Cu at (86.2, 134.4)
- added TP1: Test_Point, TestPoint:TestPoint_Pad_D1.0mm, B.Cu at (122.7, 98.8)
- added TP1: Test_Point, TestPoint:TestPoint_Pad_D1.0mm, B.Cu at (122.7, 115.3)
- added TP1: Test_Point, TestPoint:TestPoint_Pad_D1.0mm, B.Cu at (122.7, 131.8)
- added TP1: Test_Point, TestPoint:TestPoint_Pad_D1.0mm, B.Cu at (86.7, 98.8)
- added TP1: Test_Point, TestPoint:TestPoint_Pad_D1.0mm, B.Cu at (86.7, 115.3)
- added TP1: Test_Point, TestPoint:TestPoint_Pad_D1.0mm, B.Cu at (86.7, 131.8)
- added TP2: Test_Point, TestPoint:TestPoint_Pad_D1.0mm, B.Cu at (122.7, 133.8)
- added TP2: Test_Point, TestPoint:TestPoint_Pad_D1.0mm, B.Cu at (122.7, 117.3)
- added TP2: Test_Point, TestPoint:TestPoint_Pad_D1.0mm, B.Cu at (122.7, 100.8)
- added TP2: Test_Point, TestPoint:TestPoint_Pad_D1.0mm, B.Cu at (86.7, 100.8)
- added TP2: Test_Point, TestPoint:TestPoint_Pad_D1.0mm, B.Cu at (86.7, 117.3)
- added TP2: Test_Point, TestPoint:TestPoint_Pad_D1.0mm, B.Cu at (86.7, 133.8)
- added TP3: Test_Point, TestPoint:TestPoint_Pad_D1.0mm, B.Cu at (120.7, 131.8)
- added TP3: Test_Point, TestPoint:TestPoint_Pad_D1.0mm, B.Cu at (120.7, 115.3)
- added TP3: Test_Point, TestPoint:TestPoint_Pad_D1.0mm, B.Cu at (120.7, 98.8)
- added TP3: Test_Point, TestPoint:TestPoint_Pad_D1.0mm, B.Cu at (84.7, 98.8)
- added TP3: Test_Point, TestPoint:TestPoint_Pad_D1.0mm, B.Cu at (84.7, 115.3)
- added TP3: Test_Point, TestPoint:TestPoint_Pad_D1.0mm, B.Cu at (84.7, 131.8)
- added TP4: Test_Point, TestPoint:TestPoint_Pad_D1.0mm, B.Cu at (120.7, 133.8)
- added TP4: Test_Point, TestPoint:TestPoint_Pad_D1.0mm, B.Cu at (120.7, 117.3)
- added TP4: Test_Point, TestPoint:TestPoint_Pad_D1.0mm, B.Cu at (120.7, 100.8)
- added TP4: Test_Point, TestPoint:TestPoint_Pad_D1.0mm, B.Cu at (84.7, 100.8)
- added TP4: Test_Point, TestPoint:TestPoint_Pad_D1.0mm, B.Cu at (84.7, 117.3)
- added TP4: Test_Point, TestPoint:TestPoint_Pad_D1.0mm, B.Cu at (84.7, 133.8)
- added U1: NUF8401MNT4G, dfn:DFN-16-1EP_1.6x4mm_P0.5mm, F.Cu at (134.2, 120.0)
- added U1: NUF8401MNT4G, dfn:DFN-16-1EP_1.6x4mm_P0.5mm, F.Cu at (134.2, 136.5)
- added U1: NUF8401MNT4G, dfn:DFN-16-1EP_1.6x4mm_P0.5mm, F.Cu at (134.2, 103.5)
- added U1: NUF8401MNT4G, dfn:DFN-16-1EP_1.6x4mm_P0.5mm, F.Cu at (98.2, 103.5)
- added U1: NUF8401MNT4G, dfn:DFN-16-1EP_1.6x4mm_P0.5mm, F.Cu at (98.2, 120.0)
- added U1: NUF8401MNT4G, dfn:DFN-16-1EP_1.6x4mm_P0.5mm, F.Cu at (98.2, 136.5)
- added U2: MIC5245-3.3YM5, sot:SOT-23-5, F.Cu at (119.2, 136.7)
- added U2: MIC5245-3.3YM5, sot:SOT-23-5, F.Cu at (119.2, 120.2)
- added U2: MIC5245-3.3YM5, sot:SOT-23-5, F.Cu at (119.2, 103.7)
- added U2: MIC5245-3.3YM5, sot:SOT-23-5, F.Cu at (83.2, 103.7)
- added U2: MIC5245-3.3YM5, sot:SOT-23-5, F.Cu at (83.2, 120.2)
- added U2: MIC5245-3.3YM5, sot:SOT-23-5, F.Cu at (83.2, 136.7)
- added U3: STM32F103CBU6, qfn:QFN-48-1EP_7x7mm_P0.5mm_EP5.15x5.15mm, F.Cu at (128.0, 135.5)
- added U3: STM32F103CBU6, qfn:QFN-48-1EP_7x7mm_P0.5mm_EP5.15x5.15mm, F.Cu at (128.0, 102.5)
- added U3: STM32F103CBU6, qfn:QFN-48-1EP_7x7mm_P0.5mm_EP5.15x5.15mm, F.Cu at (128.0, 119.0)
- added U3: STM32F103CBU6, qfn:QFN-48-1EP_7x7mm_P0.5mm_EP5.15x5.15mm, F.Cu at (92.0, 102.5)
- added U3: STM32F103CBU6, qfn:QFN-48-1EP_7x7mm_P0.5mm_EP5.15x5.15mm, F.Cu at (92.0, 119.0)
- added U3: STM32F103CBU6, qfn:QFN-48-1EP_7x7mm_P0.5mm_EP5.15x5.15mm, F.Cu at (92.0, 135.5)
- added U4: NUF2042XV6T1G, dfn:DFN-6-1EP_1.2x1.6mm_P0.5mm, F.Cu at (119.2, 132.0)
- added U4: NUF2042XV6T1G, dfn:DFN-6-1EP_1.2x1.6mm_P0.5mm, F.Cu at (119.2, 99.0)
- added U4: NUF2042XV6T1G, dfn:DFN-6-1EP_1.2x1.6mm_P0.5mm, F.Cu at (119.2, 115.5)
- added U4: NUF2042XV6T1G, dfn:DFN-6-1EP_1.2x1.6mm_P0.5mm, F.Cu at (83.2, 99.0)
- added U4: NUF2042XV6T1G, dfn:DFN-6-1EP_1.2x1.6mm_P0.5mm, F.Cu at (83.2, 115.5)
- added U4: NUF2042XV6T1G, dfn:DFN-6-1EP_1.2x1.6mm_P0.5mm, F.Cu at (83.2, 132.0)
- added Y1: PRQC8.00CR1010V00L, crystals:Resonator_3pin_3.2x1.3mm, F.Cu at (126.5, 108.1)
- added Y1: PRQC8.00CR1010V00L, crystals:Resonator_3pin_3.2x1.3mm, F.Cu at (126.5, 124.6)
- added Y1: PRQC8.00CR1010V00L, crystals:Resonator_3pin_3.2x1.3mm, F.Cu at (126.5, 141.1)
- added Y1: PRQC8.00CR1010V00L, crystals:Resonator_3pin_3.2x1.3mm, F.Cu at (90.5, 108.1)
- added Y1: PRQC8.00CR1010V00L, crystals:Resonator_3pin_3.2x1.3mm, F.Cu at (90.5, 124.6)
- added Y1: PRQC8.00CR1010V00L, crystals:Resonator_3pin_3.2x1.3mm, F.Cu at (90.5, 141.1)
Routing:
- net (no net): track 3511.9 -> 1754.0 mm, vias 760 -> 402
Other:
- board size 131 x 113.5 mm -> 80 x 57.5 mm
